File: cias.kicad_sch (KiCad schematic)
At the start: 68 parts, among them CN13 KEYBOARD, CN6 SERIAL_DB25M, CN7 PARALLEL_DB25F, J90 DRIVE_SWITCHER, J99 CONN_HDACT, Q501 2N3904, Q502 2N3906, Q503 2N3906, Q711 2N3904, Q99 2N3906, U38 MC1488, U39 MC1489, U42 NE555, U7 VIA_8520, U8 VIA_8520

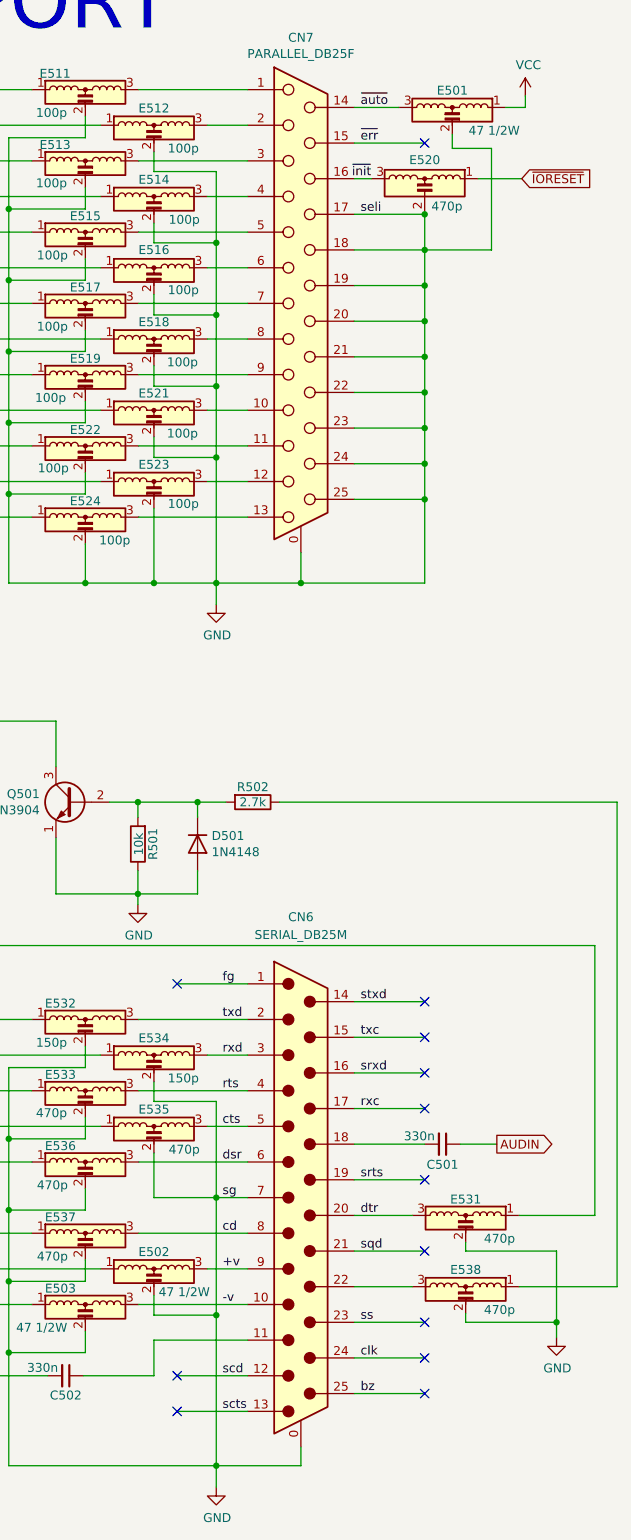
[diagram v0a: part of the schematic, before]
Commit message: belongs to previous commit, fixed schematic parity DRC errors
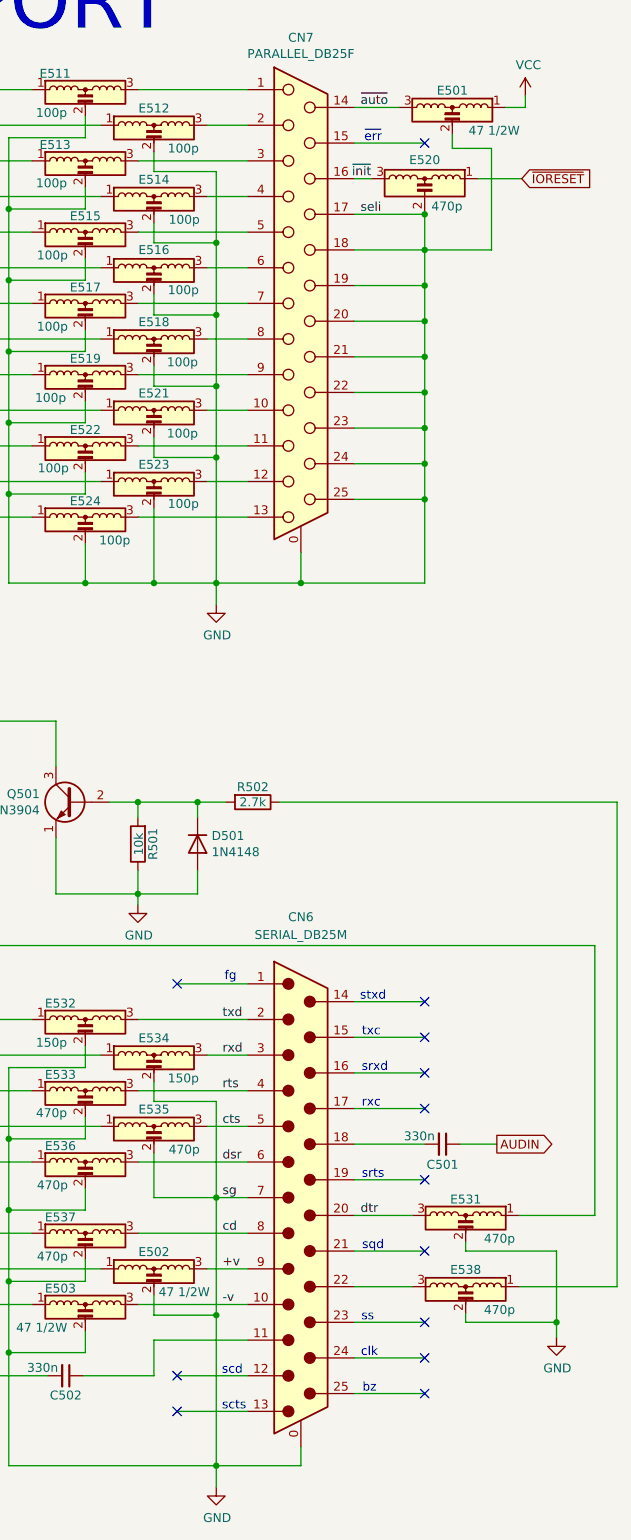
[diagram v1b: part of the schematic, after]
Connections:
- net bz: no longer names the net of CN6.25 (P25)
- net clk: no longer names the net of CN6.24 (P24)
- net fg: no longer names the net of CN6.1
- net rxc: no longer names the net of CN6.17 (P17)
- net scd: no longer names the net of CN6.12
- net scts: no longer names the net of CN6.13
- net sqd: no longer names the net of CN6.21 (P21)
- net srts: no longer names the net of CN6.19 (P19)
- net srxd: no longer names the net of CN6.16 (P16)
- net ss: no longer names the net of CN6.23 (P23)
- net stxd: no longer names the net of CN6.14 (P14)
- net txc: no longer names the net of CN6.15 (P15)
- net ~{err}: no longer names the net of CN7.15 (P15)
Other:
- note added: "bz"
- note added: "clk"
- note added: "fg"
- note added: "rxc"
- note added: "scd"
- note added: "scts"
- note added: "sqd"
- note added: "srts"
- note added: "srxd"
- note added: "ss"
- note added: "stxd"
- note added: "txc"
- note added: "~{err}"
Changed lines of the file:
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@@
 		(comment 4 "Licensed under CC BY-NC-SA 4.0")
 	)
+	(text "rxc"
+		(exclude_from_sim no)
+		(at 245.11 179.832 0)
+		(effects
+			(font
+				(size 1.27 1.27)
+			)
+		)
+	)
 	(text "ADDITIONAL CIRCUIT TO BLINK THE\nFLOPPY LED ON HARD DISK ACTIVITY\n\nCONNECT TO PIN 39 OF CF ADAPTERS"
 		(exclude_from_sim no)
@@
 		)
 	)
+	(text "scts"
+		(exclude_from_sim no)
+		(at 225.552 223.012 0)
+		(effects
+			(font
+				(size 1.27 1.27)
+			)
+		)
+	)
+	(text "srts"
+		(exclude_from_sim no)
+		(at 245.364 189.992 0)
+		(effects
+			(font
+				(size 1.27 1.27)
+			)
+		)
+	)
+	(text "stxd"
+		(exclude_from_sim no)
+		(at 245.364 164.592 0)
+		(effects
+			(font
+				(size 1.27 1.27)
+			)
+		)
+	)
 	(text "KEYBOARD\nCONNECTOR"
 		(exclude_from_sim no)
@@
 		)
 	)
+	(text "clk"
+		(exclude_from_sim no)
+		(at 244.856 215.392 0)
+		(effects
+			(font
+				(size 1.27 1.27)
+			)
+		)
+	)
+	(text "srxd"
+		(exclude_from_sim no)
+		(at 245.618 174.752 0)
+		(effects
+			(font
+				(size 1.27 1.27)
+			)
+		)
+	)
+	(text "ss"
+		(exclude_from_sim no)
+		(at 244.602 210.312 0)
+		(effects
+			(font
+				(size 1.27 1.27)
+			)
+		)
+	)
+	(text "scd"
+		(exclude_from_sim no)
+		(at 225.298 217.932 0)
+		(effects
+			(font
+				(size 1.27 1.27)
+			)
+		)
+	)
 	(text "POWER-UP\nRESET"
 		(exclude_from_sim no)
@@
 		)
 	)
+	(text "txc"
+		(exclude_from_sim no)
+		(at 245.11 169.672 0)
+		(effects
+			(font
+				(size 1.27 1.27)
+			)
+		)
+	)
 	(text "THIS CONNECTION IS MISSING\nON THE ORIGINAL SCHEMATICS\nBUT PRESENT ON ACTUAL\nBOARDS! (THANKS LIV2)"
 		(exclude_from_sim no)
@@
 		)
 	)
+	(text "sqd"
+		(exclude_from_sim no)
+		(at 245.364 200.152 0)
+		(effects
+			(font
+				(size 1.27 1.27)
+			)
+		)
+	)
+	(text "fg"
+		(exclude_from_sim no)
+		(at 225.044 161.798 0)
+		(effects
+			(font
+				(size 1.27 1.27)
+			)
+		)
+	)
+	(text "bz"
+		(exclude_from_sim no)
+		(at 244.856 220.472 0)
+		(effects
+			(font
+				(size 1.27 1.27)
+			)
+		)
+	)
 	(text "RS232\nDECOUPLING"
 		(exclude_from_sim no)
@@
 		)
 	)
+	(text "~{err}"
+		(exclude_from_sim no)
+		(at 245.364 42.164 0)
+		(effects
+			(font
+				(size 1.27 1.27)
+			)
+		)
+	)
 	(text "RS232"
 		(exclude_from_sim no)
@@
 		)
 	)
-	(label "ss"
-		(at 243.586 211.074 0)
-		(effects
-			(font
-				(size 1.27 1.27)
-			)
-			(justify left bottom)
-		)
-	)
 	(label "d10"
 		(at 61.341 145.415 0)
@@
 		)
 	)
-	(label "srts"
-		(at 243.586 190.754 0)
-		(effects
-			(font
-				(size 1.27 1.27)
-			)
-			(justify left bottom)
-		)
-	)
-	(label "srxd"
-		(at 243.586 175.514 0)
-		(effects
-			(font
-				(size 1.27 1.27)
-			)
-			(justify left bottom)
-		)
-	)
 	(label "inuse"
 		(at 348.107 140.716 180)
@@
 		)
 	)
-	(label "~{err}"
-		(at 243.586 42.926 0)
-		(effects
-			(font
-				(size 1.27 1.27)
-			)
-			(justify left bottom)
-		)
-	)
 	(label "~{auto}"
 		(at 243.586 37.846 0)
@@
 		)
 	)
-	(label "scts"
-		(at 223.901 223.774 0)
-		(effects
-			(font
-				(size 1.27 1.27)
-			)
-			(justify left bottom)
-		)
-	)
 	(label "a11"
 		(at 61.341 154.305 0)
@@
 		)
 	)
-	(label "stxd"
-		(at 243.586 165.354 0)
-		(effects
-			(font
-				(size 1.27 1.27)
-			)
-			(justify left bottom)
-		)
-	)
 	(label "pp7"
 		(at 185.166 75.946 0)
@@
 		)
 	)
-	(label "fg"
-		(at 223.901 162.814 0)
-		(effects
-			(font
-				(size 1.27 1.27)
-			)
-			(justify left bottom)
-		)
-	)
 	(label "sel1_out"
 		(at 115.062 168.275 180)
@@
 		)
 	)
-	(label "scd"
-		(at 223.901 218.694 0)
-		(effects
-			(font
-				(size 1.27 1.27)
-			)
-			(justify left bottom)
-		)
-	)
-	(label "rxc"
-		(at 243.586 180.594 0)
-		(effects
-			(font
-				(size 1.27 1.27)
-			)
-			(justify left bottom)
-		)
-	)
 	(label "a[1..23]"
 		(at 37.338 78.994 0)
@@
 		)
 	)
-	(label "txc"
-		(at 243.586 170.434 0)
-		(effects
-			(font
-				(size 1.27 1.27)
-			)
-			(justify left bottom)
-		)
-	)
-	(label "clk"
-		(at 243.586 216.154 0)
-		(effects
-			(font
-				(size 1.27 1.27)
-			)
-			(justify left bottom)
-		)
-	)
 	(label "d[0..15]"
 		(at 41.402 57.404 0)
@@
 		)
 	)
-	(label "bz"
-		(at 243.586 221.234 0)
-		(effects
-			(font
-				(size 1.27 1.27)
-			)
-			(justify left bottom)
-		)
-	)
 	(label "a8"
 		(at 61.341 89.154 0)
 		(effects
 			(font
-				(size 1.27 1.27)
-			)
-			(justify left bottom)
-		)
-	)
-	(label "sqd"
-		(at 243.586 200.914 0)
-		(effects
-			(font

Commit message: DRAM chips replaced with SIMM module
Added logic to decode 2MB chip + 1.5MB slow
Rewired trapdoor slot
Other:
- title: Rämixx500 -> Rämixx500_max
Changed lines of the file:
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@@
 	(paper "A3")
 	(title_block
-		(title "Rämixx500")
-		(date "2021-05-23")
-		(rev "1")
+		(title "Rämixx500_max")
+		(date "2026-03-13")
+		(rev "2")
 		(company "SukkoPera")
 		(comment 1 "RS232 AND PARALLEL PORT")

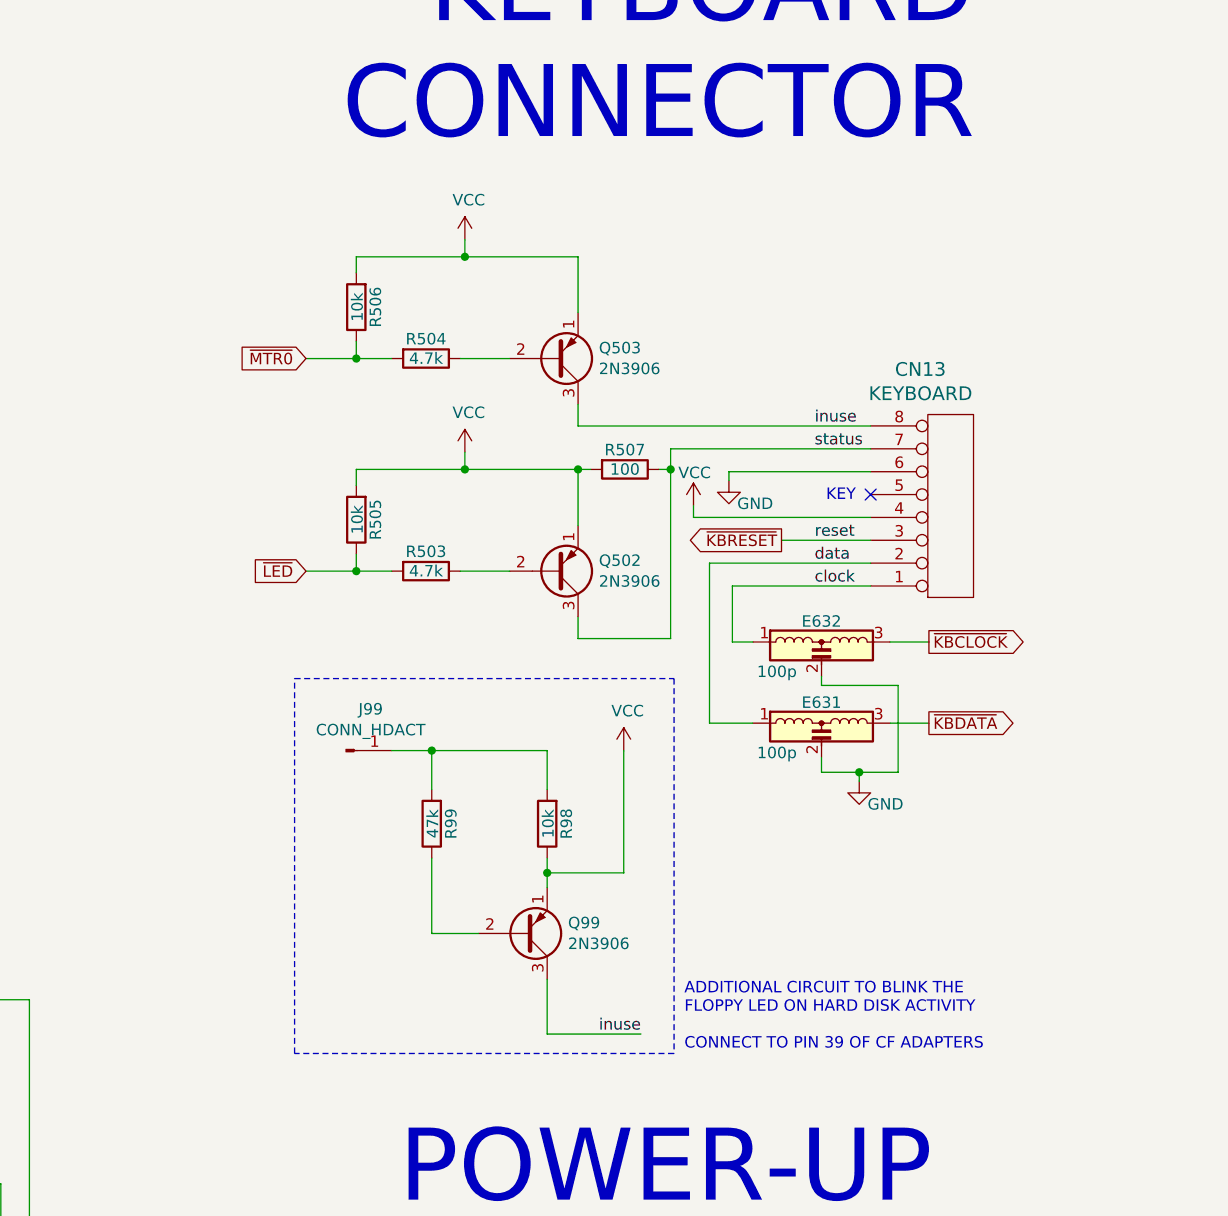
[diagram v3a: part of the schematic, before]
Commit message: Improved HDD LED circuitry so that positive drive LEDs are also supported
More routing improvements
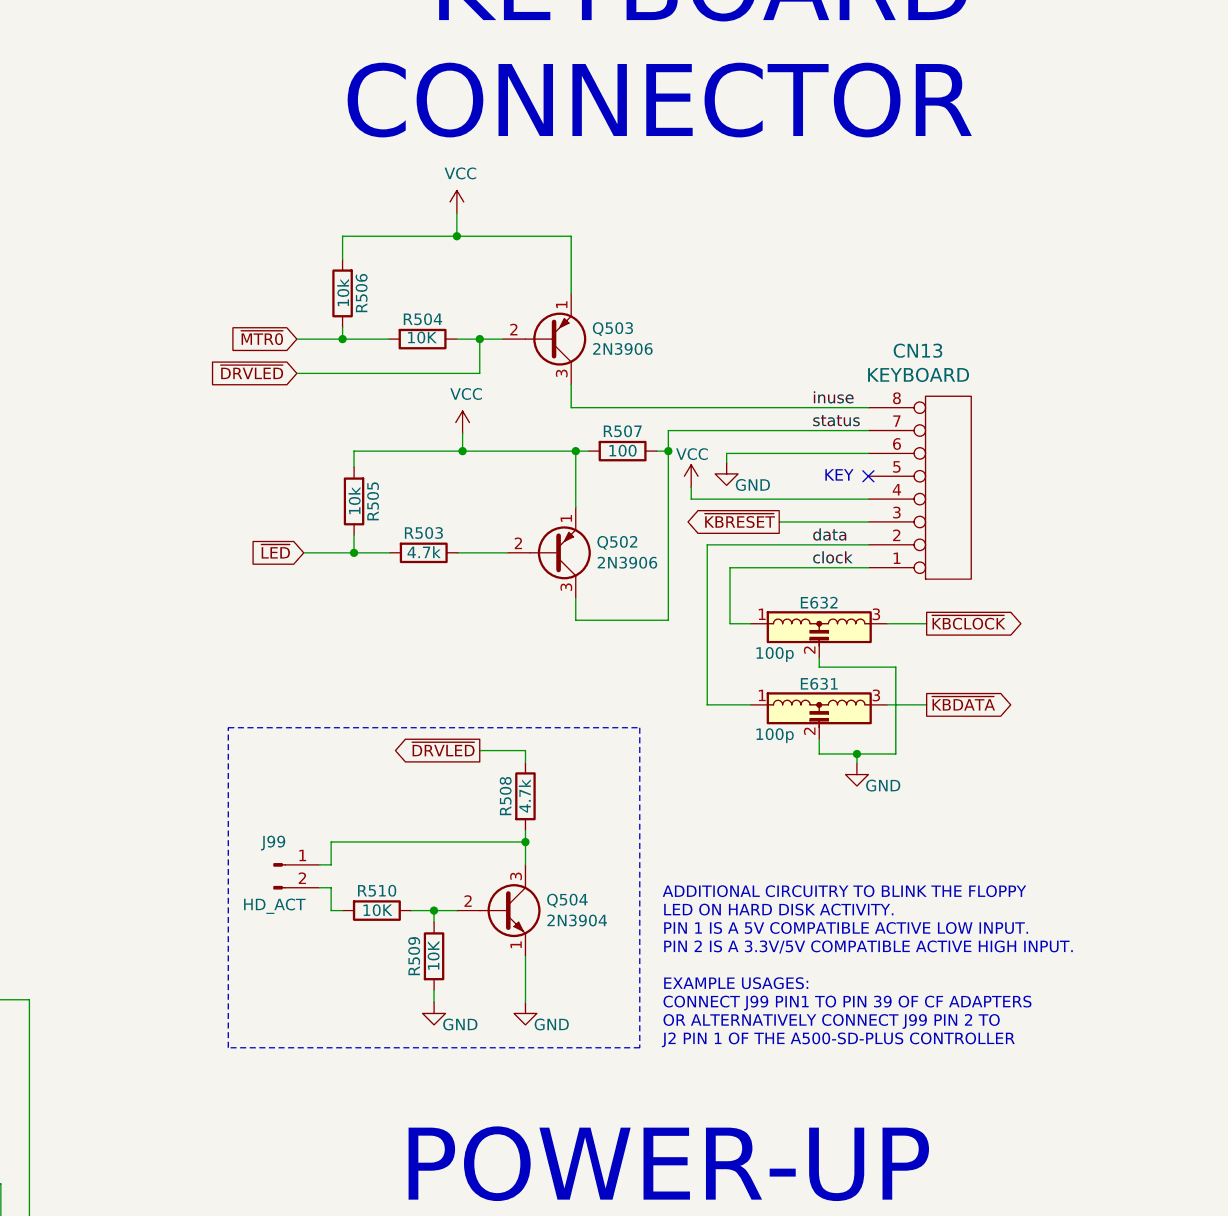
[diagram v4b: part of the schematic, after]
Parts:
- removed J99: CONN_HDACT, Raemixx500:PinHeader_1x01_P2.54mm_Vertical, symbol Connector:Conn_01x01_Male
- removed Q99: 2N3906, Package_TO_SOT_THT:TO-92L_Inline_Wide, symbol Transistor_BJT:2N3906
- removed R98: 10k, Raemixx500:R_Axial_DIN0309_L9.0mm_D3.2mm_P12.70mm_Horizontal, symbol Device:R
- removed R99: 47k, Raemixx500:R_Axial_DIN0309_L9.0mm_D3.2mm_P12.70mm_Horizontal, symbol Device:R
- added J99: HD_ACT, Connector_PinHeader_2.54mm:PinHeader_1x02_P2.54mm_Vertical, symbol Connector:Conn_01x02_Pin
- added Q504: 2N3904, Package_TO_SOT_THT:TO-92L_Inline_Wide, symbol Transistor_BJT:2N3904
- added R508: 4.7k, Raemixx500:R_Axial_DIN0309_L9.0mm_D3.2mm_P12.70mm_Horizontal, symbol Device:R
- added R509, R510: 10K, Raemixx500:R_Axial_DIN0309_L9.0mm_D3.2mm_P12.70mm_Horizontal, symbol Device:R
- R504: value 4.7k -> 10K
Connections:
- net GND: now also Q504.1 (E), R509.2
- net ~{DRVLED}: now reaches Q503.2 (B), R504.1
- net ~{DRVLED}: now also R508.1
- new net: Q504.2 (B), R509.1, R510.1
- new net: J99.2 (Pin_2), R510.2
- new net: J99.1 (Pin_1), Q504.3 (C), R508.2
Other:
- note added: "ADDITIONAL CIRCUITRY TO BLINK THE FLOPPY LED ON HARD DISK ACTIVITY. PIN 1 IS A 5V COMPATIBLE ACTIVE LOW INPUT. PIN 2 IS A 3.3V/5V COMPATIBLE ACTIVE HIGH INPUT. EXAMPLE USAGES: CONNECT J99 PIN1 TO PIN 39 OF CF ADAPTERS OR ALTERNATIVELY CONNECT J99 PIN 2 TO J2 PIN 1 OF THE A500-SD-PLUS CONTROLLER"
- note removed: "ADDITIONAL CIRCUIT TO BLINK THE FLOPPY LED ON HARD DISK ACTIVITY CONNECT TO PIN 39 OF CF ADAPTERS"
- moved on the sheet: CN13, E631, E632, Q502, Q503, R503, R504, R505, R506, R507

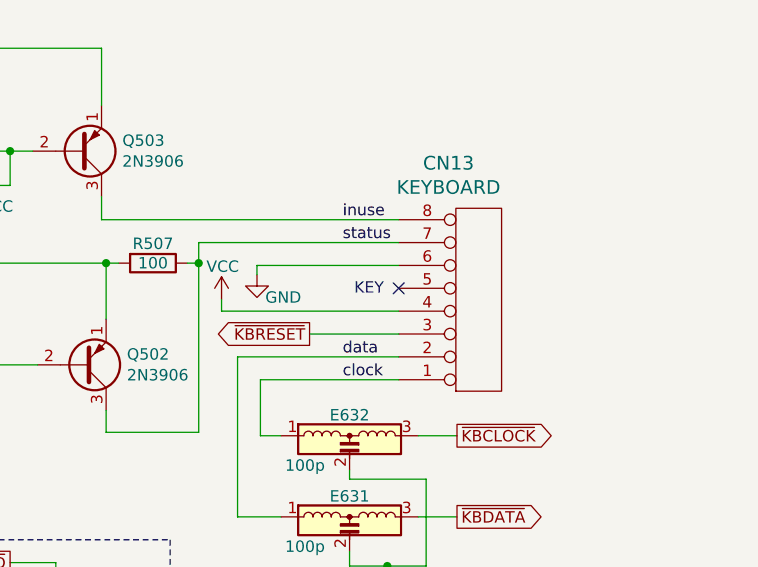
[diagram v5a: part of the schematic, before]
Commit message: added silkscreen on top for ESD diodes on bottom
added special symbol for keyboard header to get rid of schematic parity error
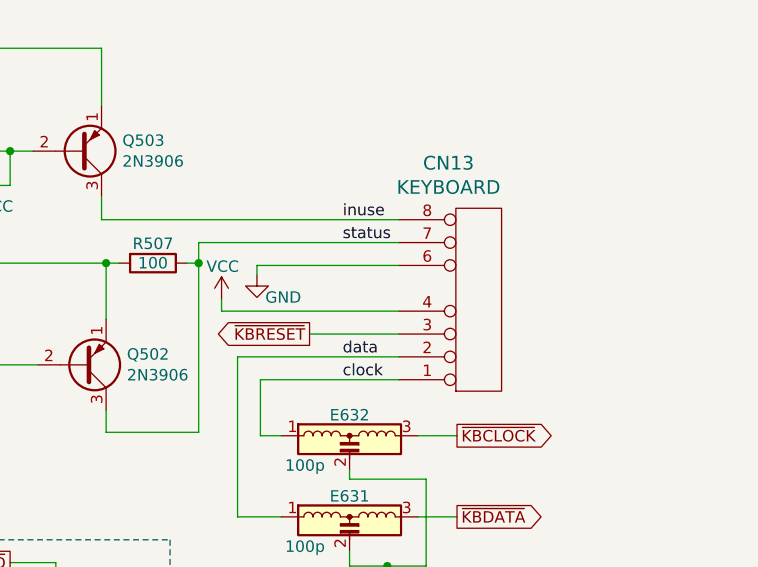
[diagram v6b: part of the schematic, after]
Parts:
- CN13: symbol conn:CONN_8 -> Raemixx:KEYBOARD_HEADER
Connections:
- no-connect marks 20 -> 19
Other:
- note removed: "KEY"
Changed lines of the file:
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@@
 		)
 	)
-	(text "KEY"
-		(exclude_from_sim no)
-		(at 368.427 79.629 0)
-		(effects
-			(font
-				(size 1.27 1.27)
-			)
-			(justify left bottom)
-		)
-	)
 	(text "~{err}"
 		(exclude_from_sim no)
@@
 	)
 	(no_connect
-		(at 373.38 78.74)
-	)
-	(no_connect
 		(at 252.73 216.154)
 	)
@@
 	)
 	(symbol
-		(lib_id "conn:CONN_8")
+		(lib_id "Raemixx:KEYBOARD_HEADER")
 		(at 382.27 80.01 0)
 		(mirror x)
@@
 		(pin "1"
 		)
-		(pin "5"
-		)
 		(pin "3"
